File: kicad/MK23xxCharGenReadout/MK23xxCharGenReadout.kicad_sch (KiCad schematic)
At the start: 136 parts, among them J1 AC IN, Q1 BC559, Q2 BC559, Q3 BC559, Q4 BC559, Q5 BC559, Q6 BC559, U1 74LS04, U2 STM32F103 BluePill, U3 74LS04, U4 MK23XX, U5 74LS138, U6 L7805, U7 74LS06, U8 74LS06, U9 L7912

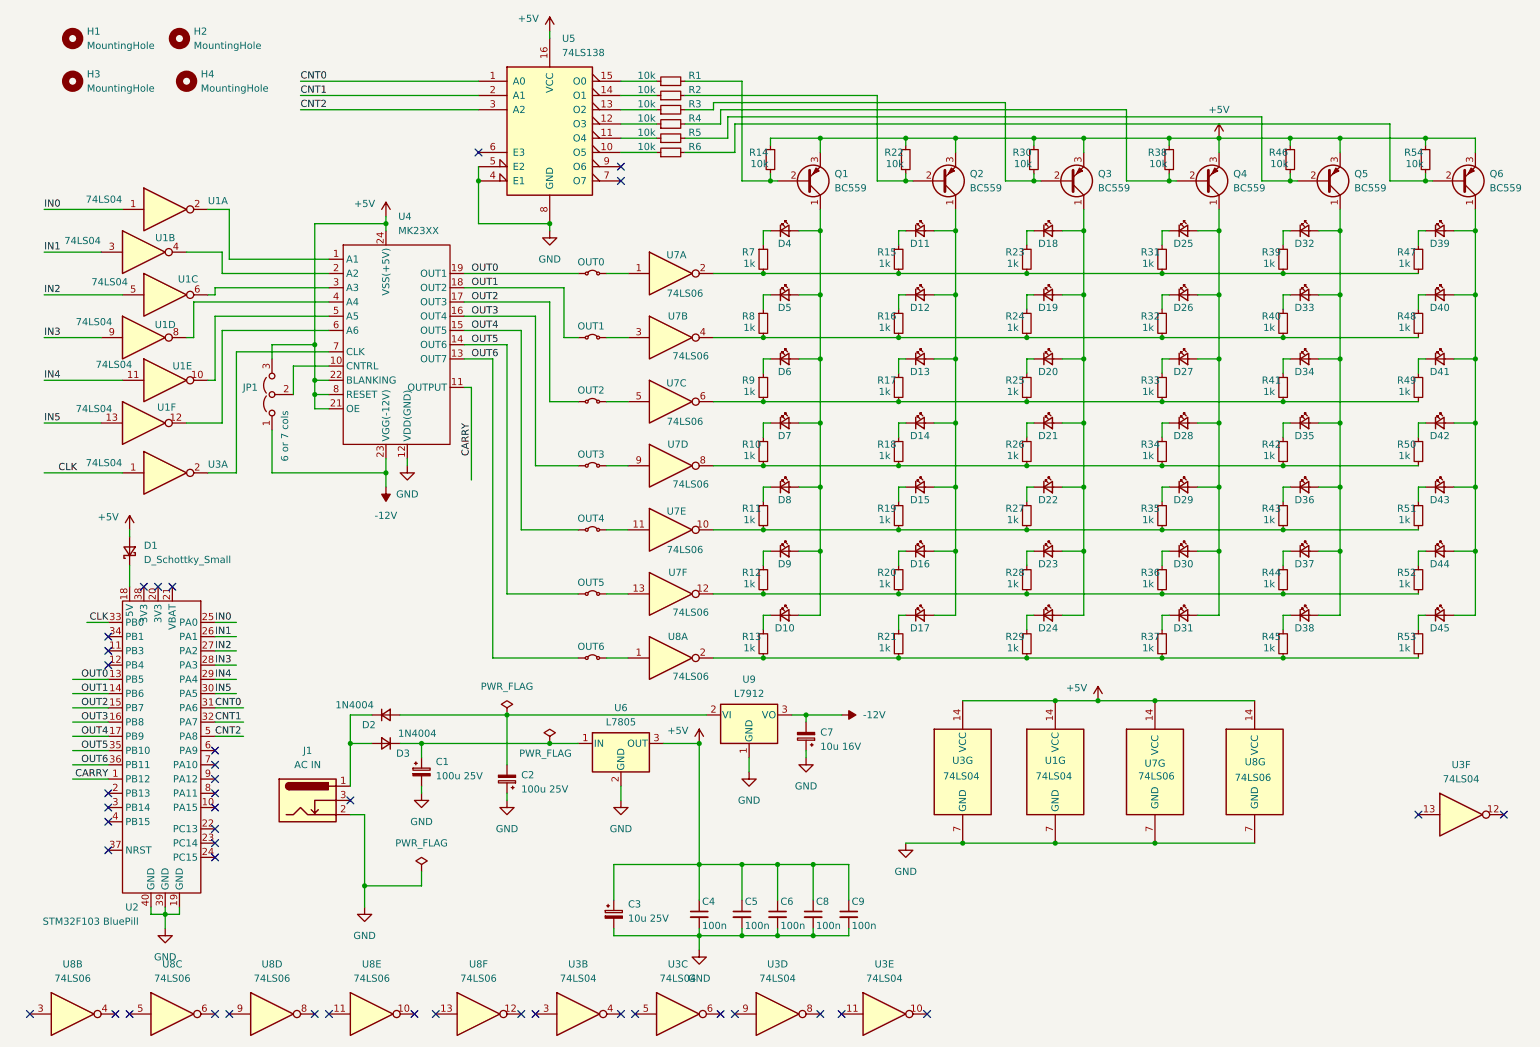
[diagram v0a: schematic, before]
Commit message: Correcting values in the schematic.
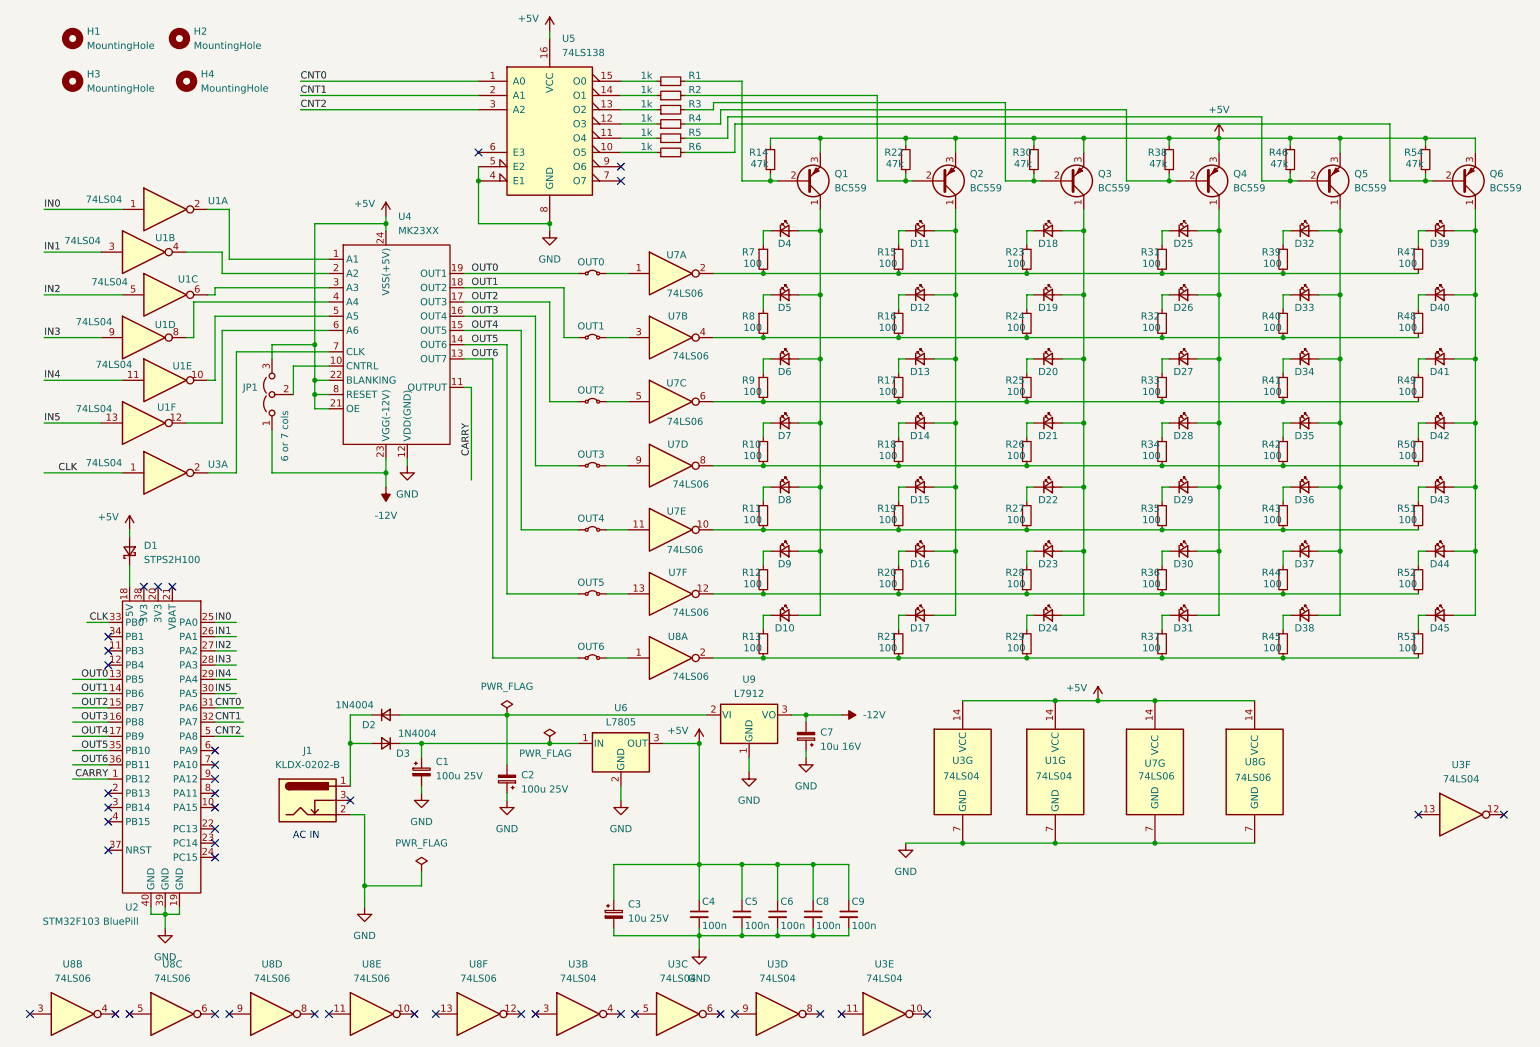
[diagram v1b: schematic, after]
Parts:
- D1: value D_Schottky_Small -> STPS2H100
- J1: value AC IN -> KLDX-0202-B
- R1, R2, R3, R4, R5, R6: value 10k -> 1k
- R10, R11, R12, R13, R15, R16, R17, R18, R19, R20, R21, R23, R24, R25, R26, R27, R28, R29, R31, R32, R33, R34, R35, R36, R37, R39, R40, R41, R42, R43, R44, R45, R47, R48, R49, R50, R51, R52, R53, R7, R8, R9: value 1k -> 100
- R14, R22, R30, R38, R46, R54: value 10k -> 47k
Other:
- note added: "AC IN"
